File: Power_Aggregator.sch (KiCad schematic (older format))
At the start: 8 parts, among them P1 XT60, P2 XT60, Q1 AUIRFS8409-7P, Q2 AUIRFS8409-7P, U1 LTC4357, U2 LTC4357

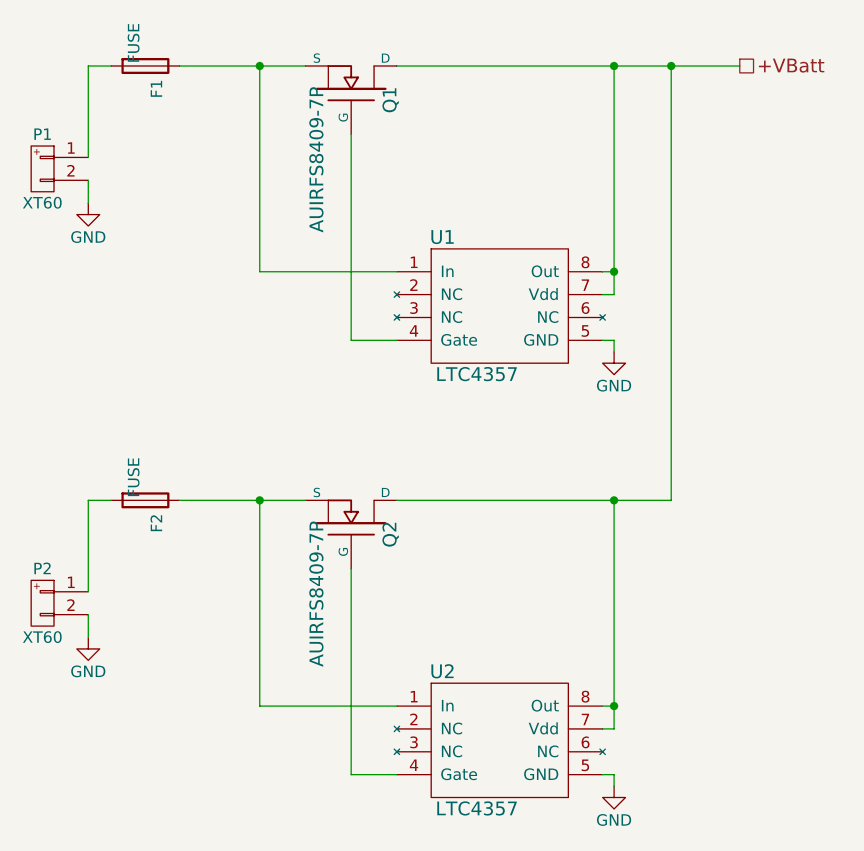
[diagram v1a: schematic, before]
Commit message: Annotate all components
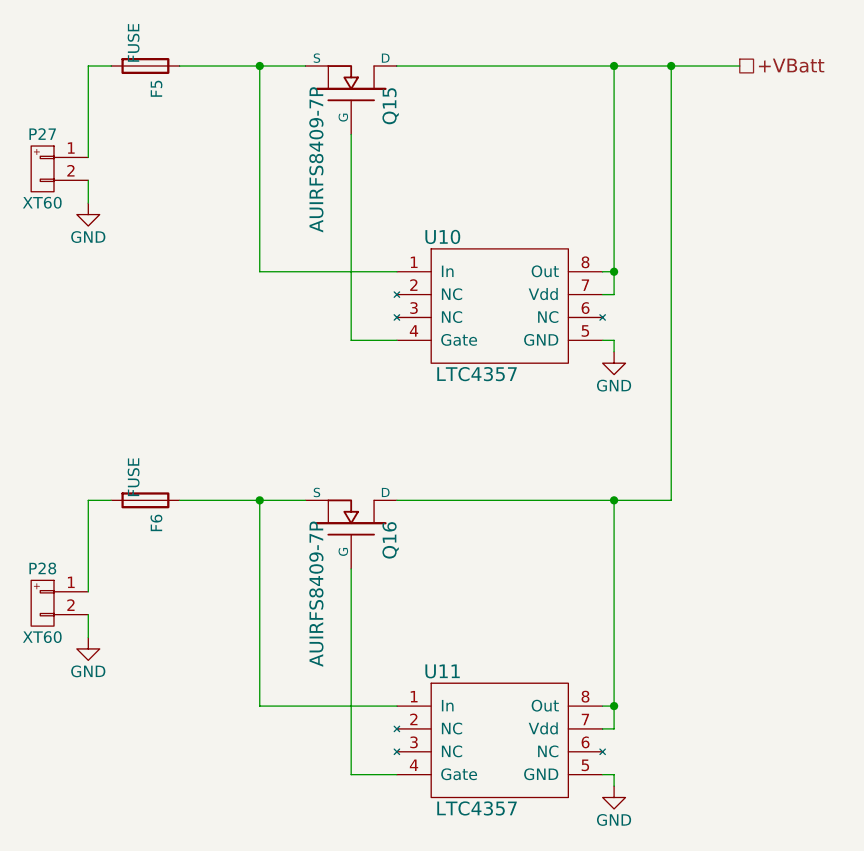
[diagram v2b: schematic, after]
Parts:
- renumbered F1 to F5, F2 to F6, P1 to P27, P2 to P28, Q1 to Q15, Q2 to Q16, U1 to U10, U2 to U11
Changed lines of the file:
@@
 LIBS:zeabus
 LIBS:ftdi
-LIBS:Power_Distributor-cache
 EELAYER 25 0
 EELAYER END
@@
 $EndDescr
 $Comp
-L Fuse F2
+L Fuse F6
 U 1 1 5626464E
 P 4300 4000
-F 0 "F2" H 4400 4050 50  0000 C CNN
+F 0 "F6" H 4400 4050 50  0000 C CNN
 F 1 "FUSE" H 4200 3950 50  0000 C CNN
 F 2 "Zeabus:FUSE_AUTO" H 4300 4000 60  0001 C CNN
@@
 $EndComp
 $Comp
-L XT60 P2
+L XT60 P28
 U 1 1 5626F4F4
 P 3850 4450
-F 0 "P2" H 3850 4600 50  0000 C CNN
+F 0 "P28" H 3850 4600 50  0000 C CNN
 F 1 "XT60" H 3850 4300 50  0000 C CNN
 F 2 "Zeabus:XT60" H 3850 4450 60  0001 C CNN
@@
 $EndComp
 $Comp
-L LTC4357 U2
+L LTC4357 U11
 U 1 1 5626F549
 P 5850 5050
-F 0 "U2" H 5600 5350 60  0000 C CNN
+F 0 "U11" H 5600 5350 60  0000 C CNN
 F 1 "LTC4357" H 5750 4750 60  0000 C CNN
 F 2 "Housings_SSOP:MSOP-8_3x3mm_Pitch0.65mm" H 5550 4900 60  0001 C CNN
@@
 $EndComp
 $Comp
-L AUIRFS8409-7P Q2
+L AUIRFS8409-7P Q16
 U 1 1 5626F582
 P 5200 4100
-F 0 "Q2" H 5210 4270 60  0000 R CNN
+F 0 "Q16" H 5210 4270 60  0000 R CNN
 F 1 "AUIRFS8409-7P" H 5210 3950 60  0000 R CNN
 F 2 "Zeabus:D2PAK-7" H 5200 4100 60  0001 C CNN
@@
 $EndComp
 $Comp
-L GND #PWR01
+L GND #PWR050
 U 1 1 5626F752
 P 6350 5250
-F 0 "#PWR01" H 6350 5000 50  0001 C CNN
+F 0 "#PWR050" H 6350 5000 50  0001 C CNN
 F 1 "GND" H 6350 5100 50  0000 C CNN
 F 2 "" H 6350 5250 60  0000 C CNN
@@
 $EndComp
 $Comp
-L GND #PWR02
+L GND #PWR051
 U 1 1 5626F76E
 P 4050 4600
-F 0 "#PWR02" H 4050 4350 50  0001 C CNN
+F 0 "#PWR051" H 4050 4350 50  0001 C CNN
 F 1 "GND" H 4050 4450 50  0000 C CNN
 F 2 "" H 4050 4600 60  0000 C CNN
@@
 	4050 4500 4050 4600
 $Comp
-L Fuse F1
+L Fuse F5
 U 1 1 5626F941
 P 4300 2100
-F 0 "F1" H 4400 2150 50  0000 C CNN
+F 0 "F5" H 4400 2150 50  0000 C CNN
 F 1 "FUSE" H 4200 2050 50  0000 C CNN
 F 2 "Zeabus:FUSE_AUTO" H 4300 2100 60  0001 C CNN
@@
 $EndComp
 $Comp
-L XT60 P1
+L XT60 P27
 U 1 1 5626F947
 P 3850 2550
-F 0 "P1" H 3850 2700 50  0000 C CNN
+F 0 "P27" H 3850 2700 50  0000 C CNN
 F 1 "XT60" H 3850 2400 50  0000 C CNN
 F 2 "Zeabus:XT60" H 3850 2550 60  0001 C CNN
@@
 $EndComp
 $Comp
-L LTC4357 U1
+L LTC4357 U10
 U 1 1 5626F94D
 P 5850 3150
-F 0 "U1" H 5600 3450 60  0000 C CNN
+F 0 "U10" H 5600 3450 60  0000 C CNN
 F 1 "LTC4357" H 5750 2850 60  0000 C CNN
 F 2 "Housings_SSOP:MSOP-8_3x3mm_Pitch0.65mm" H 5550 3000 60  0001 C CNN
@@
 $EndComp
 $Comp
-L AUIRFS8409-7P Q1
+L AUIRFS8409-7P Q15
 U 1 1 5626F953
 P 5200 2200
-F 0 "Q1" H 5210 2370 60  0000 R CNN
+F 0 "Q15" H 5210 2370 60  0000 R CNN
 F 1 "AUIRFS8409-7P" H 5210 2050 60  0000 R CNN
 F 2 "Zeabus:D2PAK-7" H 5200 2200 60  0001 C CNN
@@
 $EndComp
 $Comp
-L GND #PWR03
+L GND #PWR052
 U 1 1 5626F959
 P 6350 3350
-F 0 "#PWR03" H 6350 3100 50  0001 C CNN
+F 0 "#PWR052" H 6350 3100 50  0001 C CNN
 F 1 "GND" H 6350 3200 50  0000 C CNN
 F 2 "" H 6350 3350 60  0000 C CNN
@@
 $EndComp
 $Comp
-L GND #PWR04
+L GND #PWR053
 U 1 1 5626F95F
 P 4050 2700
-F 0 "#PWR04" H 4050 2450 50  0001 C CNN
+F 0 "#PWR053" H 4050 2450 50  0001 C CNN
 F 1 "GND" H 4050 2550 50  0000 C CNN
 F 2 "" H 4050 2700 60  0000 C CNN

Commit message: Bug fixed and clean-up for PCB generating
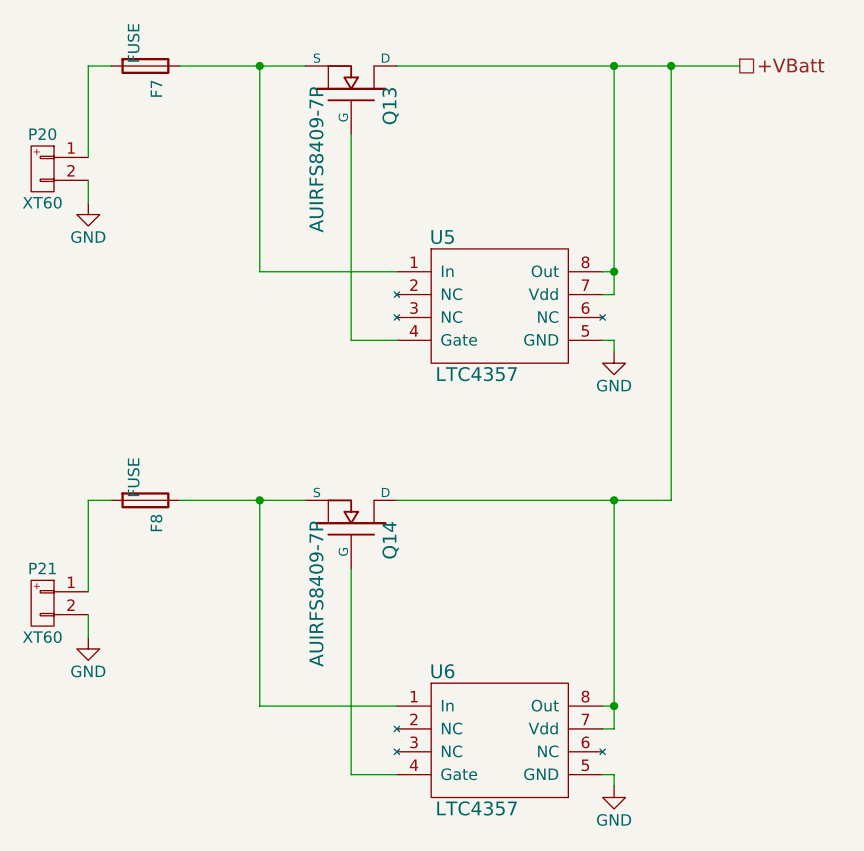
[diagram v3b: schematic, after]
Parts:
- renumbered F5 to F7, F6 to F8, P27 to P20, P28 to P21, Q15 to Q13, Q16 to Q14, U10 to U5, U11 to U6
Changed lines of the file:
@@
 $Descr A4 11693 8268
 encoding utf-8
-Sheet 13 13
+Sheet 13 10
 Title "Power Aggregator"
-Date "2017-03-14"
+Date "2017-04-06"
 Rev "1.0.0"
 Comp ""
@@
 $EndDescr
 $Comp
-L Fuse F6
+L Fuse F8
 U 1 1 5626464E
 P 4300 4000
-F 0 "F6" H 4400 4050 50  0000 C CNN
+F 0 "F8" H 4400 4050 50  0000 C CNN
 F 1 "FUSE" H 4200 3950 50  0000 C CNN
 F 2 "Zeabus:FUSE_AUTO" H 4300 4000 60  0001 C CNN
@@
 $EndComp
 $Comp
-L XT60 P28
+L XT60 P21
 U 1 1 5626F4F4
 P 3850 4450
-F 0 "P28" H 3850 4600 50  0000 C CNN
+F 0 "P21" H 3850 4600 50  0000 C CNN
 F 1 "XT60" H 3850 4300 50  0000 C CNN
 F 2 "Zeabus:XT60" H 3850 4450 60  0001 C CNN
@@
 $EndComp
 $Comp
-L LTC4357 U11
+L LTC4357 U6
 U 1 1 5626F549
 P 5850 5050
-F 0 "U11" H 5600 5350 60  0000 C CNN
+F 0 "U6" H 5600 5350 60  0000 C CNN
 F 1 "LTC4357" H 5750 4750 60  0000 C CNN
 F 2 "Housings_SSOP:MSOP-8_3x3mm_Pitch0.65mm" H 5550 4900 60  0001 C CNN
@@
 $EndComp
 $Comp
-L AUIRFS8409-7P Q16
+L AUIRFS8409-7P Q14
 U 1 1 5626F582
 P 5200 4100
-F 0 "Q16" H 5210 4270 60  0000 R CNN
+F 0 "Q14" H 5210 4270 60  0000 R CNN
 F 1 "AUIRFS8409-7P" H 5210 3950 60  0000 R CNN
 F 2 "Zeabus:D2PAK-7" H 5200 4100 60  0001 C CNN
@@
 $EndComp
 $Comp
-L GND #PWR050
+L GND #PWR49
 U 1 1 5626F752
 P 6350 5250
-F 0 "#PWR050" H 6350 5000 50  0001 C CNN
+F 0 "#PWR49" H 6350 5000 50  0001 C CNN
 F 1 "GND" H 6350 5100 50  0000 C CNN
 F 2 "" H 6350 5250 60  0000 C CNN
@@
 $EndComp
 $Comp
-L GND #PWR051
+L GND #PWR47
 U 1 1 5626F76E
 P 4050 4600
-F 0 "#PWR051" H 4050 4350 50  0001 C CNN
+F 0 "#PWR47" H 4050 4350 50  0001 C CNN
 F 1 "GND" H 4050 4450 50  0000 C CNN
 F 2 "" H 4050 4600 60  0000 C CNN
@@
 	4050 4500 4050 4600
 $Comp
-L Fuse F5
+L Fuse F7
 U 1 1 5626F941
 P 4300 2100
-F 0 "F5" H 4400 2150 50  0000 C CNN
+F 0 "F7" H 4400 2150 50  0000 C CNN
 F 1 "FUSE" H 4200 2050 50  0000 C CNN
 F 2 "Zeabus:FUSE_AUTO" H 4300 2100 60  0001 C CNN
@@
 $EndComp
 $Comp
-L XT60 P27
+L XT60 P20
 U 1 1 5626F947
 P 3850 2550
-F 0 "P27" H 3850 2700 50  0000 C CNN
+F 0 "P20" H 3850 2700 50  0000 C CNN
 F 1 "XT60" H 3850 2400 50  0000 C CNN
 F 2 "Zeabus:XT60" H 3850 2550 60  0001 C CNN
@@
 $EndComp
 $Comp
-L LTC4357 U10
+L LTC4357 U5
 U 1 1 5626F94D
 P 5850 3150
-F 0 "U10" H 5600 3450 60  0000 C CNN
+F 0 "U5" H 5600 3450 60  0000 C CNN
 F 1 "LTC4357" H 5750 2850 60  0000 C CNN
 F 2 "Housings_SSOP:MSOP-8_3x3mm_Pitch0.65mm" H 5550 3000 60  0001 C CNN
@@
 $EndComp
 $Comp
-L AUIRFS8409-7P Q15
+L AUIRFS8409-7P Q13
 U 1 1 5626F953
 P 5200 2200
-F 0 "Q15" H 5210 2370 60  0000 R CNN
+F 0 "Q13" H 5210 2370 60  0000 R CNN
 F 1 "AUIRFS8409-7P" H 5210 2050 60  0000 R CNN
 F 2 "Zeabus:D2PAK-7" H 5200 2200 60  0001 C CNN
@@
 $EndComp
 $Comp
-L GND #PWR052
+L GND #PWR48
 U 1 1 5626F959
 P 6350 3350
-F 0 "#PWR052" H 6350 3100 50  0001 C CNN
+F 0 "#PWR48" H 6350 3100 50  0001 C CNN
 F 1 "GND" H 6350 3200 50  0000 C CNN
 F 2 "" H 6350 3350 60  0000 C CNN
@@
 $EndComp
 $Comp
-L GND #PWR053
+L GND #PWR46
 U 1 1 5626F95F
 P 4050 2700
-F 0 "#PWR053" H 4050 2450 50  0001 C CNN
+F 0 "#PWR46" H 4050 2450 50  0001 C CNN
 F 1 "GND" H 4050 2550 50  0000 C CNN
 F 2 "" H 4050 2700 60  0000 C CNN
